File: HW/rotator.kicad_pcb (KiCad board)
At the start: 2 copper layers, 73.7 x 63.5 mm, 17 parts, among them J0 StepMotor_Connector, J1 Relay_Connector, J2 Generic_connector, J3 I2C_connector, J4 SPI_connector, J5 Power_connector, J6 12_IN, J7 12_OUT

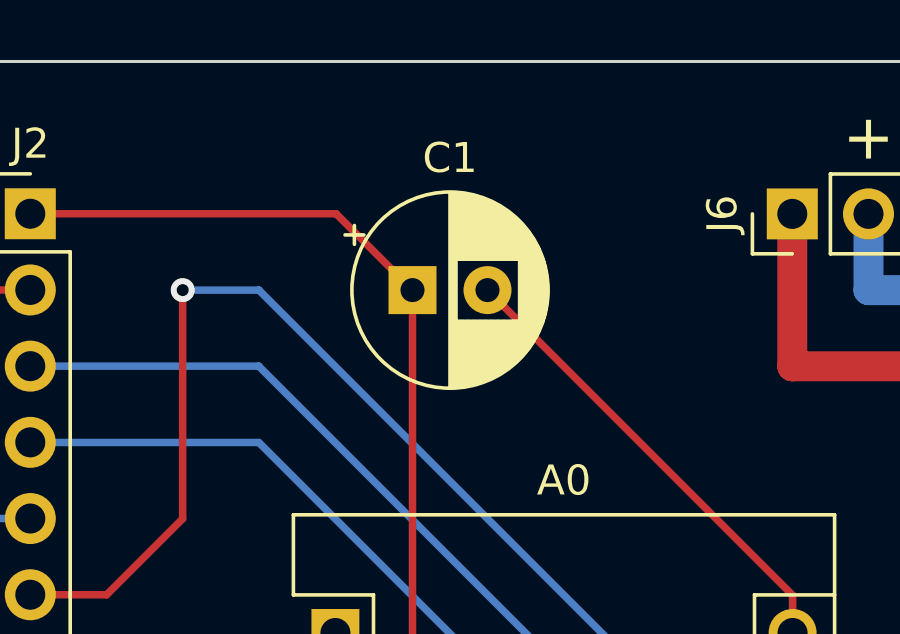
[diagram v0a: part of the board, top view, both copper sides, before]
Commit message: Fixed C1 polarization in DPS
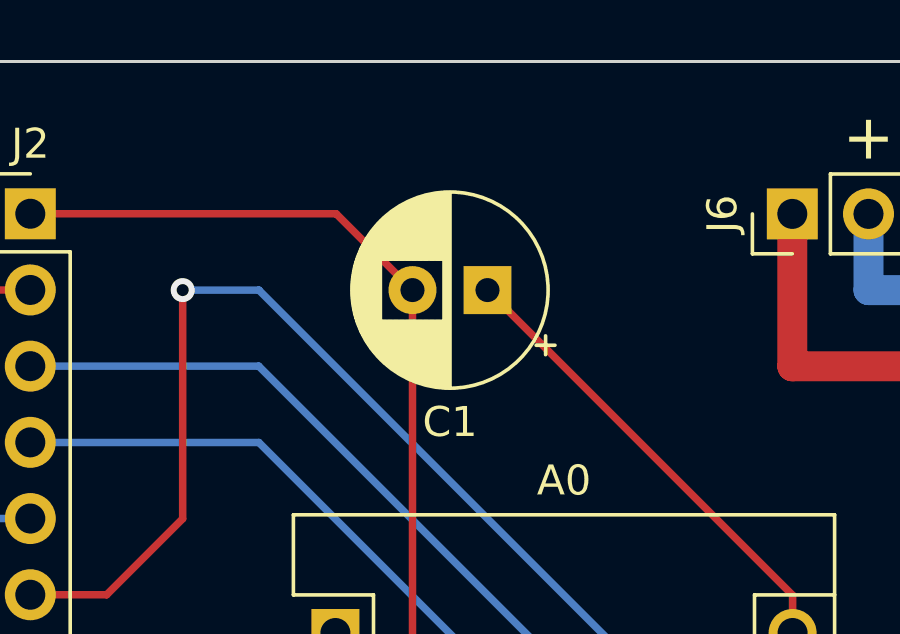
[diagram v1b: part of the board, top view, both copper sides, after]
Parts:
- moved C1 2.50 mm to (101.6, 71.1), turned to 180 degrees
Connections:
- C1 pad 1: GND -> VIN
- C1 pad 2: VIN -> GND
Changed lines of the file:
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@@
   )
   (footprint "Capacitor_THT:CP_Radial_D6.3mm_P2.50mm" (layer "F.Cu")
-    (at 99.1 71.12)
+    (at 101.6 71.12 180)
     (descr "CP, Radial series, Radial, pin pitch=2.50mm, , diameter=6.3mm, Electrolytic Capacitor")
     (tags "CP Radial series Radial pin pitch 2.50mm  diameter 6.3mm Electrolytic Capacitor")
@@
     (fp_line (start -1.443972 -1.3735) (end -0.813972 -1.3735) (layer "F.Fab") (width 0.1))
     (fp_circle (center 1.25 0) (end 4.4 0) (layer "F.Fab") (width 0.1) (fill none))
-    (pad "1" thru_hole rect (at 0 0) (size 1.6 1.6) (drill 0.8) (layers *.Cu *.Mask)
+    (pad "1" thru_hole rect (at 0 0 180) (size 1.6 1.6) (drill 0.8) (layers *.Cu *.Mask)
+      (net 28 "VIN") (pintype "passive"))
+    (pad "2" thru_hole circle (at 2.5 0 180) (size 1.6 1.6) (drill 0.8) (layers *.Cu *.Mask)
       (net 4 "GND") (pintype "passive"))
-    (pad "2" thru_hole circle (at 2.5 0) (size 1.6 1.6) (drill 0.8) (layers *.Cu *.Mask)
-      (net 28 "VIN") (pintype "passive"))
     (model "${KICAD6_3DMODEL_DIR}/Capacitor_THT.3dshapes/CP_Radial_D6.3mm_P2.50mm.wrl"
       (offset (xyz 0 0 0))
@@
   )
   (segment (start 101.61 85.09) (end 99.1 87.6) (width 0.25) (layer "F.Cu") (net 4))
-  (segment (start 99.1 71.12) (end 99.1 87.6) (width 0.25) (layer "F.Cu") (net 4))
   (segment (start 142.24 114.3) (end 138.43 110.49) (width 0.25) (layer "F.Cu") (net 4))
   (segment (start 86.36 68.575) (end 96.555 68.575) (width 0.25) (layer "F.Cu") (net 4))
   (segment (start 143.52 115.58) (end 143.52 119.38) (width 0.25) (layer "F.Cu") (net 4))
   (segment (start 111.77 85.09) (end 101.61 85.09) (width 0.25) (layer "F.Cu") (net 4))
+  (segment (start 96.555 68.575) (end 99.1 71.12) (width 0.25) (layer "F.Cu") (net 4))
   (segment (start 128.27 110.49) (end 133.34 110.49) (width 0.25) (layer "F.Cu") (net 4))
   (segment (start 86.36 118.12) (end 90.16 121.92) (width 0.25) (layer "F.Cu") (net 4))
-  (segment (start 96.555 68.575) (end 99.1 71.12) (width 0.25) (layer "F.Cu") (net 4))
   (segment (start 127 121.92) (end 128.28 120.64) (width 0.25) (layer "F.Cu") (net 4))
   (segment (start 111.77 85.09) (end 120.65 85.09) (width 0.25) (layer "F.Cu") (net 4))
@@
   (segment (start 138.43 110.49) (end 133.34 110.49) (width 0.25) (layer "F.Cu") (net 4))
   (segment (start 142.24 114.3) (end 143.52 115.58) (width 0.25) (layer "F.Cu") (net 4))
+  (segment (start 99.1 71.12) (end 99.1 87.6) (width 0.25) (layer "F.Cu") (net 4))
   (segment (start 86.36 90.17) (end 96.53 90.17) (width 0.25) (layer "F.Cu") (net 4))
   (segment (start 120.65 85.09) (end 124.46 88.9) (width 0.25) (layer "F.Cu") (net 4))

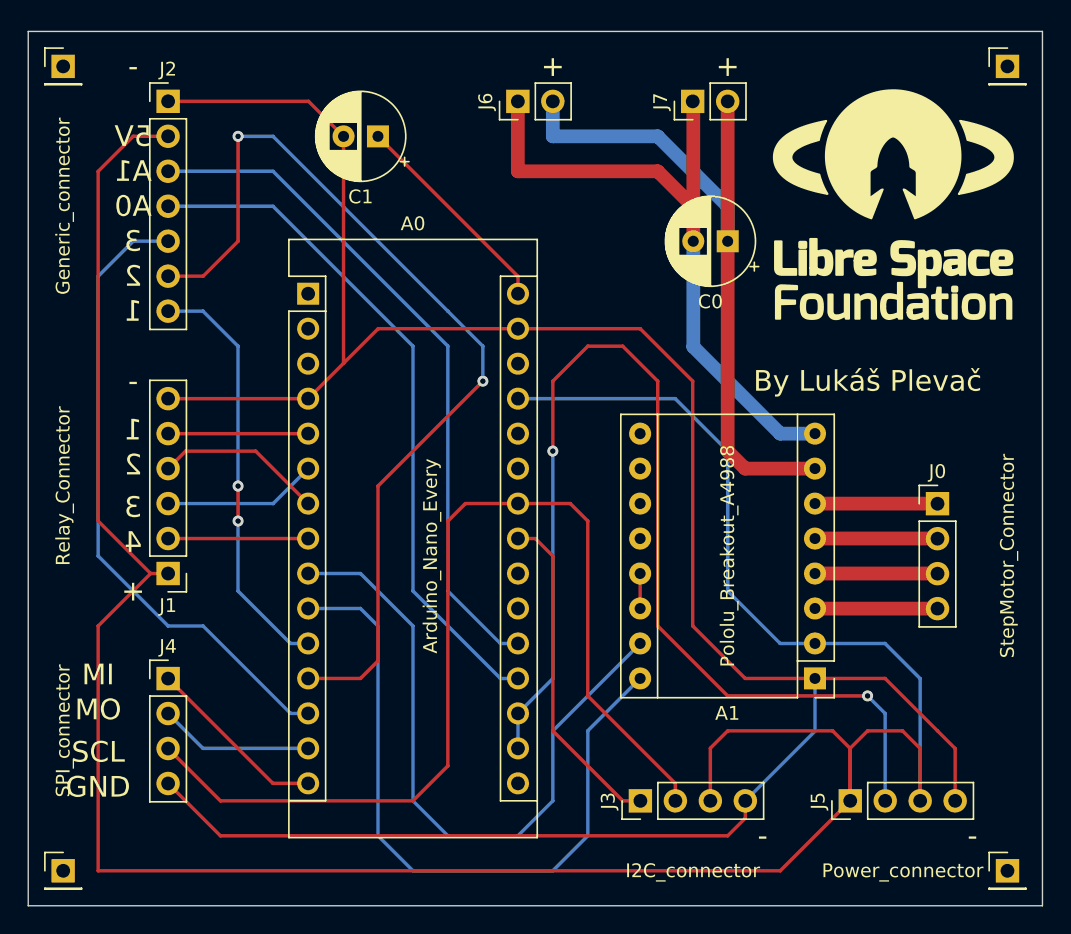
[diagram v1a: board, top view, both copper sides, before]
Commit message: Fixed capacitator C0 polarization
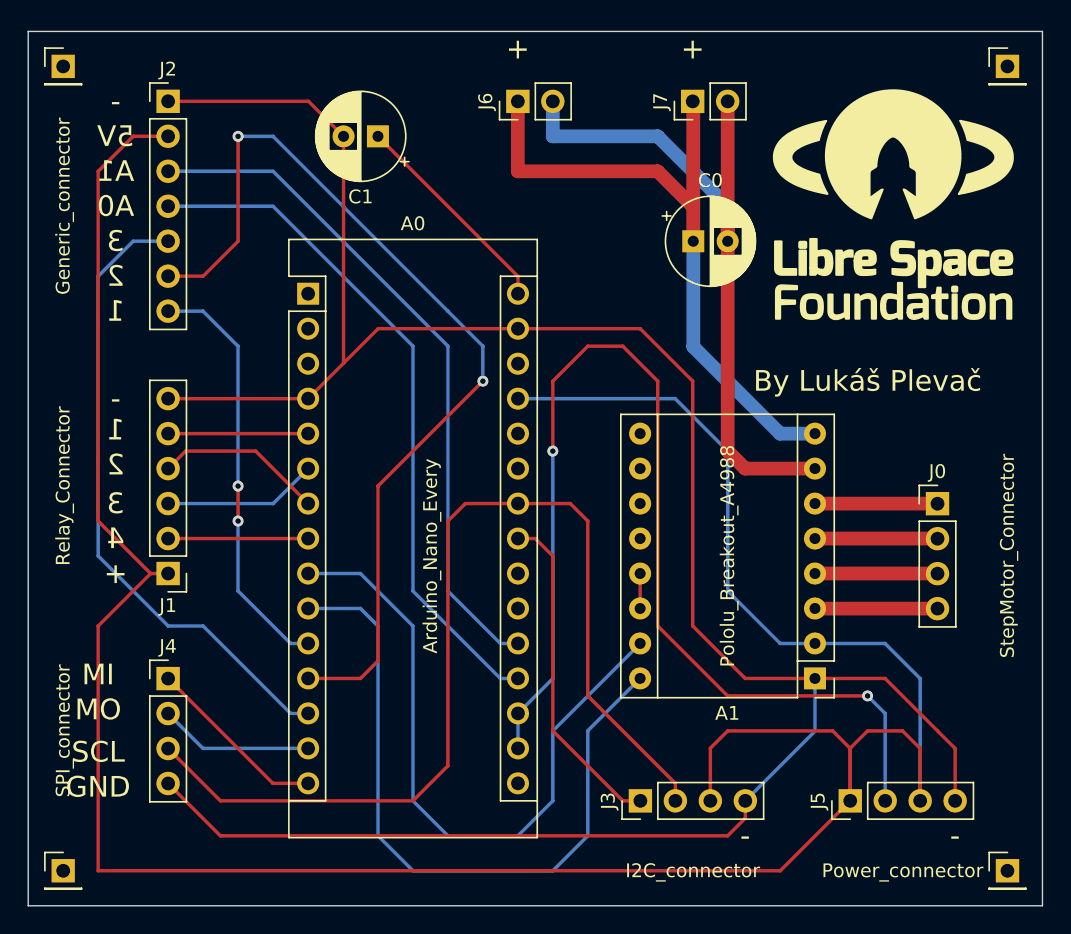
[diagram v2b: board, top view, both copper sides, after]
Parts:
- moved C0 2.50 mm to (124.5, 78.7), turned to 0 degrees
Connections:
- C0 pad 1: GND_12V -> 12V
- C0 pad 2: 12V -> GND_12V
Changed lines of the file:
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@@
   )
   (footprint "Capacitor_THT:CP_Radial_D6.3mm_P2.50mm" (layer "F.Cu")
-    (at 127 78.74 180)
+    (at 124.5 78.74)
     (descr "CP, Radial series, Radial, pin pitch=2.50mm, , diameter=6.3mm, Electrolytic Capacitor")
     (tags "CP Radial series Radial pin pitch 2.50mm  diameter 6.3mm Electrolytic Capacitor")
@@
     (fp_line (start -1.128972 -1.6885) (end -1.128972 -1.0585) (layer "F.Fab") (width 0.1))
     (fp_circle (center 1.25 0) (end 4.4 0) (layer "F.Fab") (width 0.1) (fill none))
-    (pad "1" thru_hole rect (at 0 0 180) (size 1.6 1.6) (drill 0.8) (layers *.Cu *.Mask)
-      (net 33 "GND_12V") (pintype "passive"))
-    (pad "2" thru_hole circle (at 2.5 0 180) (size 1.6 1.6) (drill 0.8) (layers *.Cu *.Mask)
+    (pad "1" thru_hole rect (at 0 0) (size 1.6 1.6) (drill 0.8) (layers *.Cu *.Mask)
       (net 34 "12V") (pintype "passive"))
+    (pad "2" thru_hole circle (at 2.5 0) (size 1.6 1.6) (drill 0.8) (layers *.Cu *.Mask)
+      (net 33 "GND_12V") (pintype "passive"))
     (model "${KICAD6_3DMODEL_DIR}/Capacitor_THT.3dshapes/CP_Radial_D6.3mm_P2.50mm.wrl"
       (offset (xyz 0 0 0))
@@
   (gr_line (start 76.2 63.5) (end 149.86 63.5) (layer "Edge.Cuts") (width 0.1))
   (gr_line (start 149.86 127) (end 76.2 127) (layer "Edge.Cuts") (width 0.1))
-  (gr_text "-" (at 83.82 66.04) (layer "F.SilkS")
+  (gr_text "-" (at 82.55 68.58) (layer "F.SilkS")
     (effects (font (size 1.5 1.5) (thickness 0.3)) (justify mirror))
   )
-  (gr_text "-" (at 83.82 88.9) (layer "F.SilkS")
+  (gr_text "-" (at 82.55 90.17) (layer "F.SilkS")
     (effects (font (size 1.5 1.5) (thickness 0.3)) (justify mirror))
   )
-  (gr_text "3\n" (at 83.82 78.74) (layer "F.SilkS")
+  (gr_text "3\n" (at 82.55 78.74) (layer "F.SilkS")
     (effects (font (size 1.5 1.5) (thickness 0.3)) (justify mirror))
   )
@@
     (effects (font (size 1.5 1.5) (thickness 0.3)))
   )
-  (gr_text "4\n" (at 83.82 100.6) (layer "F.SilkS")
+  (gr_text "4\n" (at 82.55 100.33) (layer "F.SilkS")
     (effects (font (size 1.5 1.5) (thickness 0.3)) (justify mirror))
   )
-  (gr_text "-" (at 144.78 121.92) (layer "F.SilkS")
+  (gr_text "-" (at 143.51 121.92) (layer "F.SilkS")
     (effects (font (size 1.5 1.5) (thickness 0.3)) (justify mirror))
   )
-  (gr_text "2" (at 83.82 81.28) (layer "F.SilkS")
+  (gr_text "2" (at 82.55 81.28) (layer "F.SilkS")
     (effects (font (size 1.5 1.5) (thickness 0.3)) (justify mirror))
   )
-  (gr_text "2" (at 83.82 94.98) (layer "F.SilkS")
+  (gr_text "2" (at 82.55 94.98) (layer "F.SilkS")
     (effects (font (size 1.5 1.5) (thickness 0.3)) (justify mirror))
   )
-  (gr_text "5V\n" (at 83.82 71.12) (layer "F.SilkS")
+  (gr_text "5V\n" (at 82.55 71.12) (layer "F.SilkS")
     (effects (font (size 1.5 1.5) (thickness 0.3)) (justify mirror))
   )
-  (gr_text "+" (at 114.3 66.04) (layer "F.SilkS")
+  (gr_text "+" (at 111.76 64.77) (layer "F.SilkS")
     (effects (font (size 1.5 1.5) (thickness 0.3)) (justify mirror))
   )
-  (gr_text "1" (at 83.82 92.44) (layer "F.SilkS")
+  (gr_text "1" (at 82.55 92.44) (layer "F.SilkS")
     (effects (font (size 1.5 1.5) (thickness 0.3)) (justify mirror))
   )
-  (gr_text "-" (at 129.54 121.92) (layer "F.SilkS")
+  (gr_text "-" (at 128.27 121.92) (layer "F.SilkS")
     (effects (font (size 1.5 1.5) (thickness 0.3)) (justify mirror))
   )
-  (gr_text "1\n" (at 83.82 83.82) (layer "F.SilkS")
+  (gr_text "1\n" (at 82.55 83.82) (layer "F.SilkS")
     (effects (font (size 1.5 1.5) (thickness 0.3)) (justify mirror))
   )
@@
     (effects (font (size 1.5 1.5) (thickness 0.3)))
   )
-  (gr_text "3\n" (at 83.82 98.06) (layer "F.SilkS")
+  (gr_text "3\n" (at 82.55 97.79) (layer "F.SilkS")
     (effects (font (size 1.5 1.5) (thickness 0.3)) (justify mirror))
   )
-  (gr_text "A0" (at 83.82 76.2) (layer "F.SilkS")
+  (gr_text "A0" (at 82.55 76.2) (layer "F.SilkS")
     (effects (font (size 1.5 1.5) (thickness 0.3)) (justify mirror))
   )
-  (gr_text "+" (at 83.82 104.14) (layer "F.SilkS")
+  (gr_text "+" (at 82.55 102.87) (layer "F.SilkS")
     (effects (font (size 1.5 1.5) (thickness 0.3)) (justify mirror))
   )
-  (gr_text "A1" (at 83.82 73.66) (layer "F.SilkS")
+  (gr_text "A1" (at 82.55 73.66) (layer "F.SilkS")
     (effects (font (size 1.5 1.5) (thickness 0.3)) (justify mirror))
   )
@@
     (effects (font (size 1.5 1.5) (thickness 0.3)))
   )
-  (gr_text "+" (at 127 66.04) (layer "F.SilkS")
+  (gr_text "+" (at 124.46 64.77) (layer "F.SilkS")
     (effects (font (size 1.5 1.5) (thickness 0.3)) (justify mirror))
   )
